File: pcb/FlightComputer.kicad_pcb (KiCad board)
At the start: 2 copper layers, 22.9 x 63.5 mm, 80 parts, among them J1 USB4105-GF-A, J2 MOTOR L, J3 MOTOR R, J4 LED L, J7 SERVO R, J8 SERVO R, Q1 DMG3415U, Q2 Si2319CDS, Q3 Si2319CDS, Q4 MMBT3904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

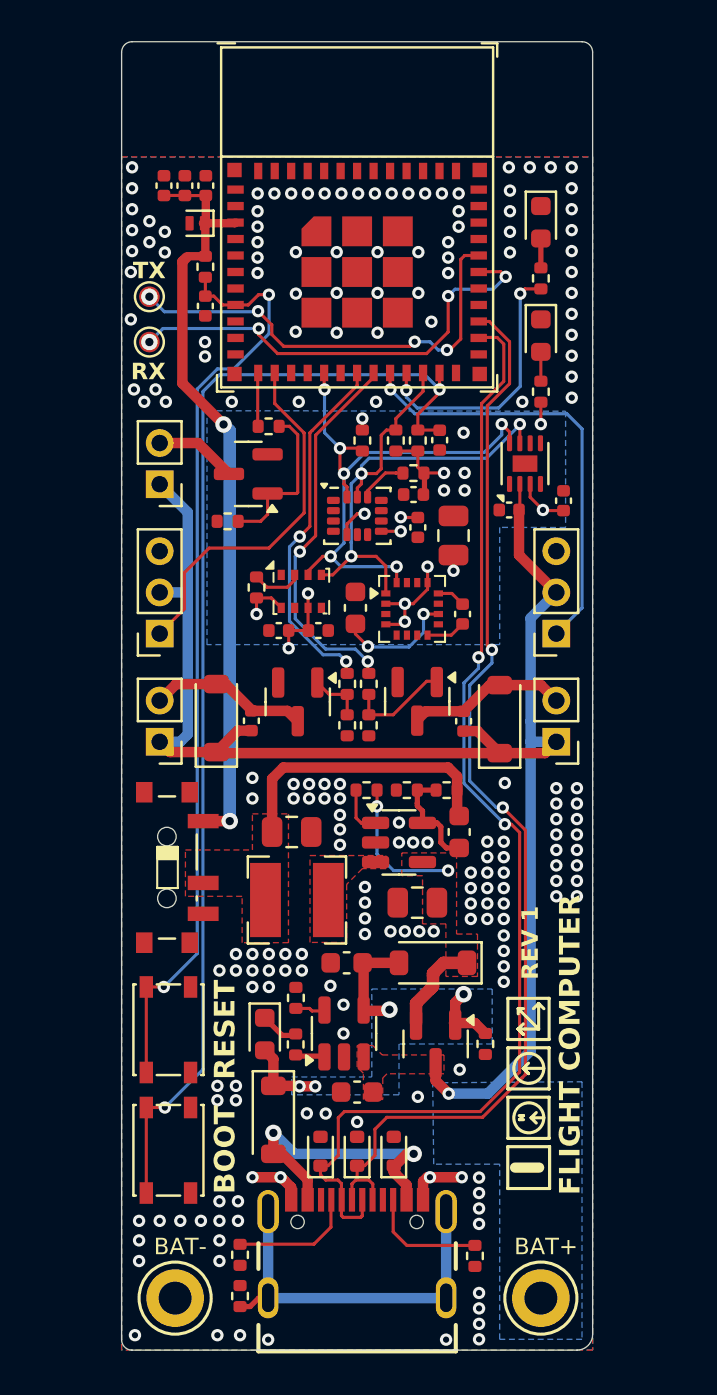
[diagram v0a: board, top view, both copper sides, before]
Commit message: Rearrange some vias, minor changes
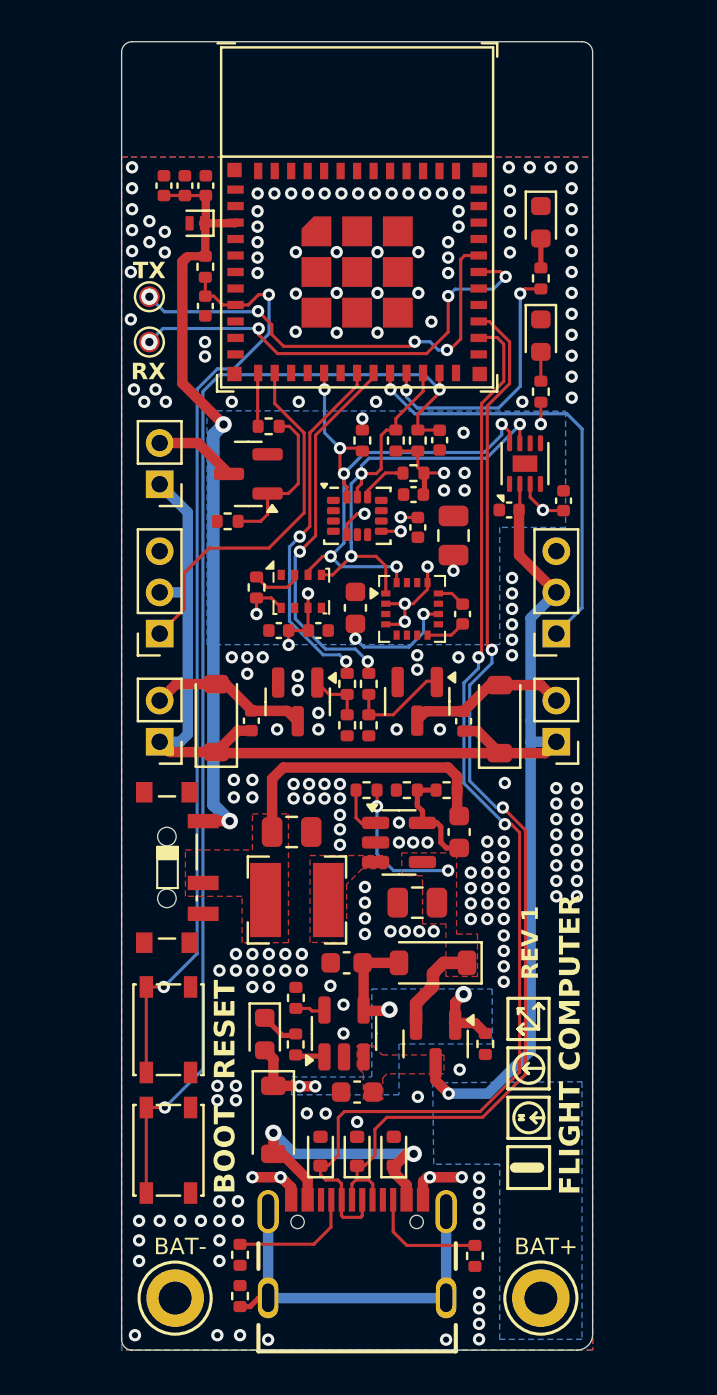
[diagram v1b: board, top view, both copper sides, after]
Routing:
- net GND: vias 195 -> 217

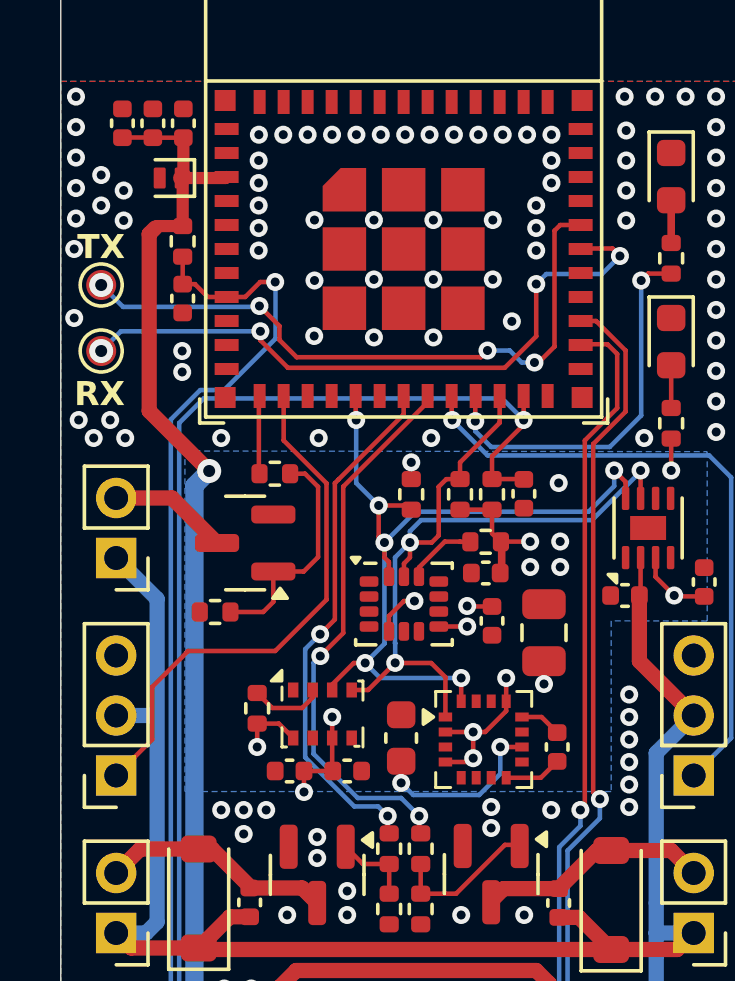
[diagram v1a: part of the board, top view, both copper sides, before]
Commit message: BMP280 > BMP388
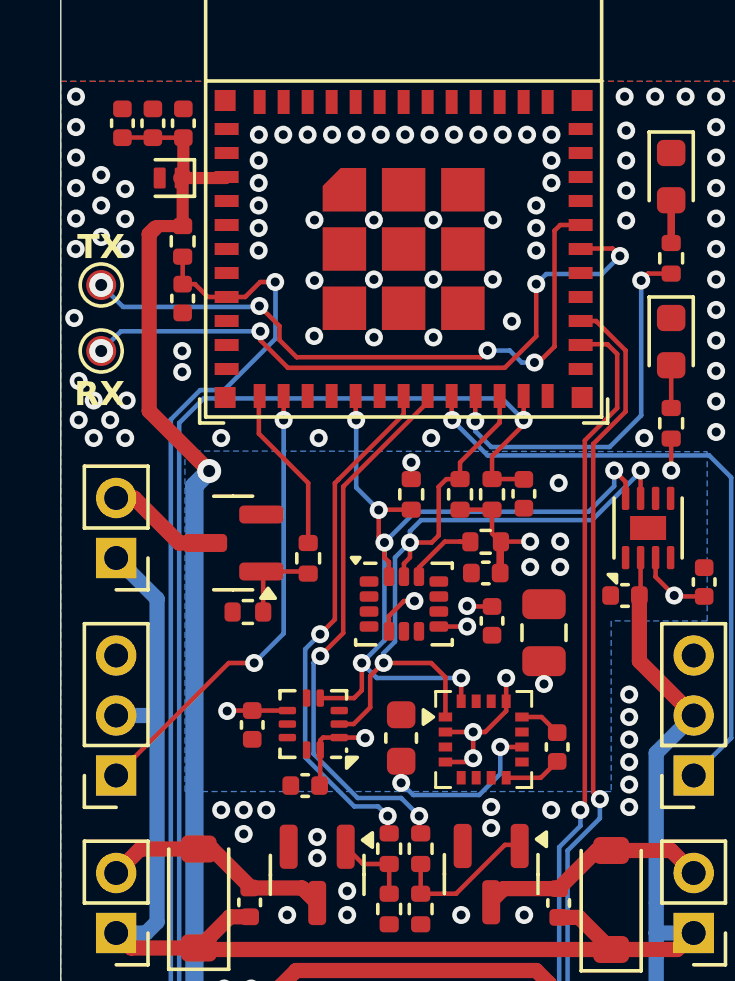
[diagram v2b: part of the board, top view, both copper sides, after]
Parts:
- removed C12: 10nF 10V, Capacitor_SMD:C_0402_1005Metric
- removed C13: 100nF 10V, Capacitor_SMD:C_0402_1005Metric
- removed R12: 10kR 1%, Resistor_SMD:R_0402_1005Metric
- removed U8: BMP280, Package_LGA:Bosch_LGA-8_2x2.5mm_P0.65mm_ClockwisePinNumbering
- added C22: 100nF 10V, Capacitor_SMD:C_0402_1005Metric, F.Cu at (144.8, 94.1)
- added C23: 100nF 10V, Capacitor_SMD:C_0402_1005Metric, F.Cu at (143.0, 92.1)
- added U1: BMP388, Package_LGA:Rohm_MLGA010V020A_LGA-10_2x2mm_P0.45mm_LayoutBorder2x3y, F.Cu at (145.1, 92.0)
- moved R22 3.03 mm to (144.9, 86.5), turned to -90 degrees
- moved R23 1.09 mm to (142.9, 88.3)
- moved Q4 0.40 mm to (142.4, 86.0)
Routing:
- net Net-(Q4-B): track 7.73 -> 2.88 mm
- net IO0: track 2.47 -> 5.65 mm
- net Net-(U8-CSB): track 2.45 -> 0.00 mm
- net IO1: track 17.8 -> 15.5 mm, vias 0 -> 2
- net IO8_SCL: track 27.1 -> 28.8 mm
- net IO10_SDA: track 27.8 -> 28.7 mm
- net +3V3: track 61.5 -> 60.9 mm, vias 16 -> 15
- net GND: vias 217 -> 222

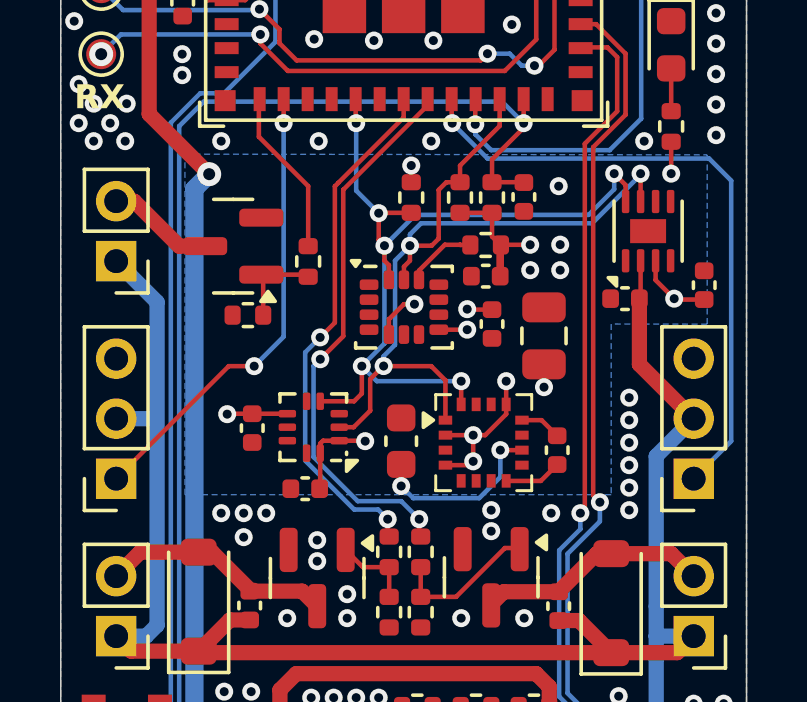
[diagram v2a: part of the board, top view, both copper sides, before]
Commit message: add a few vias, move traces
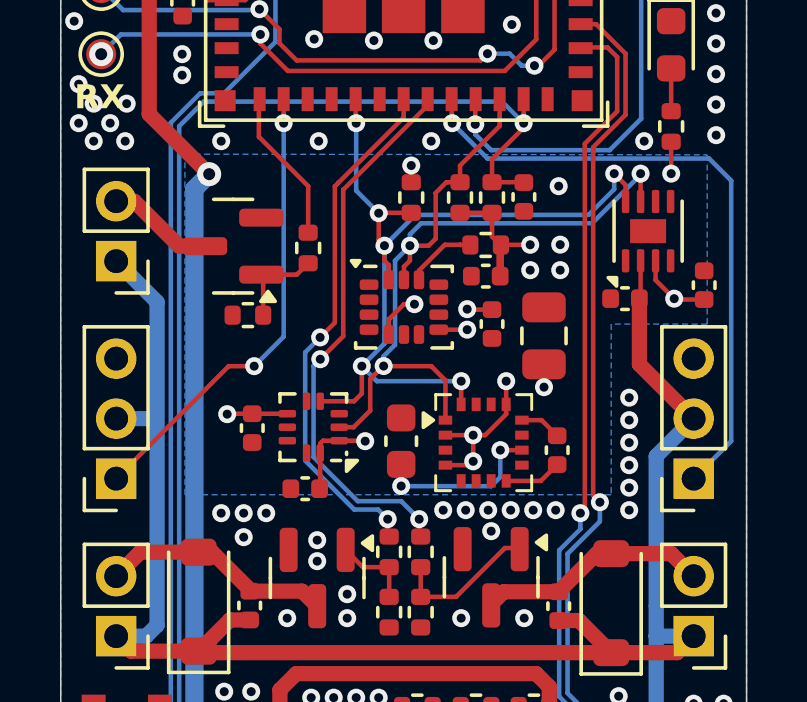
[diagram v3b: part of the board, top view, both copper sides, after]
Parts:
- moved R22 0.45 mm to (144.9, 86.1)
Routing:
- net GND: vias 222 -> 226
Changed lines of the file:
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@@
 	(footprint "Resistor_SMD:R_0402_1005Metric"
 		(layer "F.Cu")
-		(at 144.9 86.51 -90)
+		(at 144.9 86.06 -90)
 		(descr "Resistor SMD 0402 (1005 Metric), square (rectangular) end terminal, IPC_7351 nominal, (Body size source: IPC-SM-782 page 72, https://www.pcb-3d.com/wordpress/wp-content/uploads/ipc-sm-782a_amendment_1_and_2.pdf), generated with kicad-footprint-generator")
 		(tags "resistor")
@@
 		(tags "capacitor")
 		(property "Reference" "C22"
-			(at 0 -1.16 360)
+			(at 0 -1.16 0)
 			(layer "F.SilkS")
 			(hide yes)
@@
 		)
 		(property "Value" "100nF 10V"
-			(at 0 1.16 360)
+			(at 0 1.16 0)
 			(layer "F.Fab")
 			(effects
@@
 		)
 		(fp_text user "${REFERENCE}"
-			(at 0 0 360)
+			(at 0 0 0)
 			(layer "F.Fab")
 			(effects
@@
 		(tags "Rohm LGA NoLead")
 		(property "Reference" "U1"
-			(at 0 -2.15 360)
+			(at 0 -2.15 0)
 			(layer "F.SilkS")
 			(hide yes)
@@
 		)
 		(property "Value" "BMP388"
-			(at 0 1.8 360)
+			(at 0 1.8 0)
 			(layer "F.Fab")
 			(effects
@@
 		)
 		(fp_text user "${REFERENCE}"
-			(at 0 0 360)
+			(at 0 0 0)
 			(layer "F.Fab")
 			(effects
@@
 	)
 	(via
+		(at 149.4 94.8)
+		(size 0.6)
+		(drill 0.3)
+		(layers "F.Cu" "B.Cu")
+		(free yes)
+		(net 1)
+	)
+	(via
 		(at 148.463 106.807)
 		(size 0.6)
@@
 	)
 	(via
+		(at 153.15 94.8)
+		(size 0.6)
+		(drill 0.3)
+		(layers "F.Cu" "B.Cu")
+		(free yes)
+		(net 1)
+	)
+	(via
 		(at 151.6888 78.613)
 		(size 0.6)
@@
 	)
 	(via
+		(at 151.65 94.8)
+		(size 0.6)
+		(drill 0.3)
+		(layers "F.Cu" "B.Cu")
+		(free yes)
+		(net 1)
+	)
+	(via
 		(at 139.5 122.25)
 		(size 0.6)
@@
 	)
 	(via
-		(at 151 94.8)
+		(at 150.9 94.8)
 		(size 0.6)
 		(drill 0.3)
@@
 	)
 	(via
+		(at 152.4 94.8)
+		(size 0.6)
+		(drill 0.3)
+		(layers "F.Cu" "B.Cu")
+		(free yes)
+		(net 1)
+	)
+	(via
 		(at 154.4 103.85)
 		(size 0.6)
@@
 	)
 	(via
+		(at 150.15 94.8)
+		(size 0.6)
+		(drill 0.3)
+		(layers "F.Cu" "B.Cu")
+		(free yes)
+		(net 1)
+	)
+	(via
 		(at 154.4 106.85)
 		(size 0.6)
@@
 	)
 	(via
-		(at 153 94.9)
-		(size 0.6)
-		(drill 0.3)
-		(layers "F.Cu" "B.Cu")
-		(free yes)
-		(net 1)
-	)
-	(via
 		(at 155.448 71.12)
 		(size 0.6)
@@
 	(segment
 		(start 144.9 84)
-		(end 144.9 86)
+		(end 144.9 85.55)
 		(width 0.1524)
 		(layer "F.Cu")
@@
 	)
 	(segment
-		(start 143.256 81.026)
-		(end 143.256 82.356)
+		(start 143.256 82.356)
+		(end 144.9 84)
 		(width 0.1524)
 		(layer "F.Cu")
@@
 	)
 	(segment
-		(start 143.256 82.356)
-		(end 144.9 84)
+		(start 143.256 81.026)
+		(end 143.256 82.356)
 		(width 0.1524)
 		(layer "F.Cu")
@@
 	)
 	(segment
+		(start 149.15 85.75)
+		(end 148.916 85.984)
+		(width 0.1524)
+		(layer "F.Cu")
+		(net 20)
+	)
+	(segment
 		(start 147.418031 90)
 		(end 149 90)
@@
 	)
 	(segment
+		(start 151.282 81.1)
+		(end 151.282 81.994)
+		(width 0.1524)
+		(layer "F.Cu")
+		(net 20)
+	)
+	(segment
 		(start 149.475 90.475)
 		(end 149.475 91.8)
@@
 	)
 	(segment
-		(start 149.2504 84.1248)
-		(end 149.2504 85.7496)
+		(start 146.415 92.035)
+		(end 145.935 92.035)
 		(width 0.1524)
 		(layer "F.Cu")
@@
 	)
 	(segment
-		(start 146.415 92.035)
-		(end 145.935 92.035)
+		(start 149.5044 83.8708)
+		(end 149.15 84.2252)
+		(width 0.1524)
+		(layer "F.Cu")
+		(net 20)
+	)
+	(segment
+		(start 148.916 85.984)
+		(end 148.292 85.984)
 		(width 0.1524)
 		(layer "F.Cu")
@@
 	)
 	(segment
-		(start 149.5044 83.8708)
-		(end 149.2504 84.1248)
+		(start 149.9616 83.3144)
+		(end 149.9616 83.8708)
 		(width 0.1524)
 		(layer "F.Cu")
@@
 	)
 	(segment
-		(start 151.282 81.1)
-		(end 151.282 81.994)
-		(width 0.1524)
-		(layer "F.Cu")
-		(net 20)
-	)
-	(segment
-		(start 149.2504 85.7496)
-		(end 149.016 85.984)
+		(start 149.9616 83.8708)
+		(end 149.5044 83.8708)
 		(width 0.1524)
 		(layer "F.Cu")
@@
 	)
 	(segment
-		(start 149.9616 83.3144)
-		(end 149.9616 83.8708)
-		(width 0.1524)
-		(layer "F.Cu")
-		(net 20)
-	)
-	(segment
 		(start 148.292 86.484)
 		(end 148.292 85.984)
@@
 	)
 	(segment
-		(start 149.016 85.984)
-		(end 148.292 85.984)
+		(start 149.15 84.2252)
+		(end 149.15 85.75)
 		(width 0.1524)
 		(layer "F.Cu")
@@
 		(net 20)
 	)
-	(segment
-		(start 149.9616 83.8708)
-		(end 149.5044 83.8708)
-		(width 0.1524)
-		(layer "F.Cu")
-		(net 20)
-	)
 	(via
 		(at 155.98 83.5826)
@@
 	)
 	(segment
-		(start 150.6 94.4)
+		(start 151 94)
 		(end 151.304928 93.695072)
 		(width 0.1524)
@@
 	)
 	(segment
-		(start 148 93.9968)
-		(end 148.4032 94.4)
+		(start 151.304928 93.695072)
+		(end 151.304928 92.798905)
 		(width 0.1524)
 		(layer "B.Cu")
@@
 	)
 	(segment
-		(start 151.304928 93.695072)
-		(end 151.304928 92.798905)
+		(start 148 93.9968)
+		(end 148.0032 94)
 		(width 0.1524)
 		(layer "B.Cu")
@@
 	)
 	(segment
-		(start 148.4032 94.4)
-		(end 150.6 94.4)
+		(start 148.0032 94)
+		(end 151 94)
 		(width 0.1524)
 		(layer "B.Cu")
@@
 	)
 	(segment
-		(start 144.9 87.02)
-		(end 144.83 86.95)
+		(start 143.4 86.95)
+		(end 143.4 88.3)
 		(width 0.1524)
 		(layer "F.Cu")
@@
 	)
 	(segment
-		(start 143.4 86.95)
-		(end 143.4 88.3)
+		(start 144.52 86.95)
+		(end 143.4 86.95)
 		(width 0.1524)
 		(layer "F.Cu")
@@
 	)
 	(segment
-		(start 144.83 86.95)
-		(end 143.4 86.95)
+		(start 144.9 86.57)
+		(end 144.52 86.95)
 		(width 0.1524)
 		(layer "F.Cu")

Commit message: Move resistors
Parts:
- moved R23 2.39 mm to (144.9, 87.0), turned to -90 degrees
- moved R22 1.15 mm to (144.9, 84.9)
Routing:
- net IO0: track 5.20 -> 4.05 mm
- net GND: vias 226 -> 220
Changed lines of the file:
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@@
 	(footprint "Resistor_SMD:R_0402_1005Metric"
 		(layer "F.Cu")
-		(at 144.9 86.06 -90)
+		(at 144.9 84.91 -90)
 		(descr "Resistor SMD 0402 (1005 Metric), square (rectangular) end terminal, IPC_7351 nominal, (Body size source: IPC-SM-782 page 72, https://www.pcb-3d.com/wordpress/wp-content/uploads/ipc-sm-782a_amendment_1_and_2.pdf), generated with kicad-footprint-generator")
 		(tags "resistor")
@@
 	(footprint "Resistor_SMD:R_0402_1005Metric"
 		(layer "F.Cu")
-		(at 142.89 88.3 180)
+		(at 144.9 87 -90)
 		(descr "Resistor SMD 0402 (1005 Metric), square (rectangular) end terminal, IPC_7351 nominal, (Body size source: IPC-SM-782 page 72, https://www.pcb-3d.com/wordpress/wp-content/uploads/ipc-sm-782a_amendment_1_and_2.pdf), generated with kicad-footprint-generator")
 		(tags "resistor")
 		(property "Reference" "R23"
-			(at 0 -1.17 0)
+			(at 0 -1.17 90)
 			(layer "F.SilkS")
 			(hide yes)
@@
 		)
 		(property "Value" "10kR 1%"
-			(at 0 1.17 0)
+			(at 0 1.17 90)
 			(layer "F.Fab")
 			(effects
@@
 		)
 		(property "Footprint" "Resistor_SMD:R_0402_1005Metric"
-			(at 0 0 180)
+			(at 0 0 -90)
 			(unlocked yes)
 			(layer "F.Fab")
@@
 		)
 		(property "Datasheet" ""
-			(at 0 0 180)
+			(at 0 0 -90)
 			(unlocked yes)
 			(layer "F.Fab")
@@
 		)
 		(property "Description" ""
-			(at 0 0 180)
+			(at 0 0 -90)
 			(unlocked yes)
 			(layer "F.Fab")
@@
 		)
 		(property "LCSC" "C25744"
-			(at 0 0 180)
+			(at 0 0 -90)
 			(unlocked yes)
 			(layer "F.Fab")
@@
 		)
 		(fp_line
-			(start 0.93 0.47)
-			(end -0.93 0.47)
+			(start -0.93 0.47)
+			(end -0.93 -0.47)
 			(stroke
 				(width 0.05)
@@
 		)
 		(fp_line
-			(start 0.93 -0.47)
-			(end 0.93 0.47)
+			(start 0.93 0.47)
+			(end -0.93 0.47)
 			(stroke
 				(width 0.05)
@@
 		)
 		(fp_line
-			(start -0.93 0.47)
-			(end -0.93 -0.47)
+			(start -0.93 -0.47)
+			(end 0.93 -0.47)
 			(stroke
 				(width 0.05)
@@
 		)
 		(fp_line
-			(start -0.93 -0.47)
-			(end 0.93 -0.47)
+			(start 0.93 -0.47)
+			(end 0.93 0.47)
 			(stroke
 				(width 0.05)
@@
 		)
 		(fp_line
-			(start 0.525 0.27)
-			(end -0.525 0.27)
+			(start -0.525 0.27)
+			(end -0.525 -0.27)
 			(stroke
 				(width 0.1)
@@
 		)
 		(fp_line
-			(start 0.525 -0.27)
-			(end 0.525 0.27)
+			(start 0.525 0.27)
+			(end -0.525 0.27)
 			(stroke
 				(width 0.1)
@@
 		)
 		(fp_line
-			(start -0.525 0.27)
-			(end -0.525 -0.27)
+			(start -0.525 -0.27)
+			(end 0.525 -0.27)
 			(stroke
 				(width 0.1)
@@
 		)
 		(fp_line
-			(start -0.525 -0.27)
-			(end 0.525 -0.27)
+			(start 0.525 -0.27)
+			(end 0.525 0.27)
 			(stroke
 				(width 0.1)
@@
 		)
 		(fp_text user "${REFERENCE}"
-			(at 0 0 0)
+			(at 0 0 90)
 			(layer "F.Fab")
 			(effects
@@
 		)
 		(pad "1" smd roundrect
-			(at -0.51 0 180)
+			(at -0.51 0 270)
 			(size 0.54 0.64)
 			(layers "F.Cu" "F.Paste" "F.Mask")
@@
 		)
 		(pad "2" smd roundrect
-			(at 0.51 0 180)
+			(at 0.51 0 270)
 			(size 0.54 0.64)
 			(layers "F.Cu" "F.Paste" "F.Mask")
@@
 			)
 		)
+		(property "LCSC" "C779278"
+			(at 0 0 180)
+			(unlocked yes)
+			(layer "F.Fab")
+			(hide yes)
+			(effects
+				(font
+					(size 1 1)
+					(thickness 0.15)
+				)
+			)
+		)
 		(sheetname "Root")
 		(sheetfile "FlightComputer.kicad_sch")
@@
 	)
 	(via
-		(at 137.75 81.25)
-		(size 0.6)
-		(drill 0.3)
-		(layers "F.Cu" "B.Cu")
-		(free yes)
-		(net 1)
-	)
-	(via
 		(at 151.0538 75.2348)
 		(size 0.6)
@@
 	)
 	(via
-		(at 137.15 76.2)
-		(size 0.6)
-		(drill 0.3)
-		(layers "F.Cu" "B.Cu")
-		(free yes)
-		(net 1)
-	)
-	(via
 		(at 152.1 98.4)
 		(size 0.6)
@@
 	)
 	(via
-		(at 138.8 76.2)
-		(size 0.6)
-		(drill 0.3)
-		(layers "F.Cu" "B.Cu")
-		(free yes)
-		(net 1)
-	)
-	(via
-		(at 138.85 81.25)
-		(size 0.6)
-		(drill 0.3)
-		(layers "F.Cu" "B.Cu")
-		(free yes)
-		(net 1)
-	)
-	(via
 		(at 138 73.734)
 		(size 0.6)
@@
 	)
 	(via
-		(at 138 75.8)
-		(size 0.6)
-		(drill 0.3)
-		(layers "F.Cu" "B.Cu")
-		(free yes)
-		(net 1)
-	)
-	(via
 		(at 142.1 101.7)
 		(size 0.6)
@@
 	)
 	(via
-		(at 137.25 80.6)
-		(size 0.6)
-		(drill 0.3)
-		(layers "F.Cu" "B.Cu")
-		(free yes)
-		(net 1)
-	)
-	(via
 		(at 155.5 72.25)
 		(size 0.6)
@@
 	(segment
 		(start 144.9 84)
-		(end 144.9 85.55)
+		(end 144.9 84.4)
 		(width 0.1524)
 		(layer "F.Cu")
@@
 	)
 	(segment
-		(start 143.4 86.95)
-		(end 143.4 88.3)
+		(start 144.9 86.49)
+		(end 144.9 85.42)
 		(width 0.1524)
 		(layer "F.Cu")
@@
 	)
 	(segment
-		(start 144.52 86.95)
+		(start 144.44 86.95)
 		(end 143.4 86.95)
 		(width 0.1524)
@@
 	)
 	(segment
-		(start 144.9 86.57)
-		(end 144.52 86.95)
+		(start 144.9 86.49)
+		(end 144.44 86.95)
 		(width 0.1524)
 		(layer "F.Cu")
@@
 		(polygon
 			(pts
-				(xy 158.2 88.6) (xy 155 88.5952) (xy 155 94.284) (xy 140.792 94.284) (xy 140.792 82.934) (xy 158.2 82.9564)
+				(xy 155 94.25) (xy 140.75 94.25) (xy 140.75 83) (xy 158.5 83) (xy 158.5 88.5976) (xy 155 88.5952)
 			)
 		)
